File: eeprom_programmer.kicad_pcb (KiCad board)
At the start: 2 copper layers, 80 x 80 mm, 23 parts, among them J1 AVR ISP, J2 USB_B, SW1 Reset, U1 ATmega8-16PU, U2 MCP2221AxP, U3 74HC595, U4 74HC595, U5 28C256, Y1 7,3728MHz

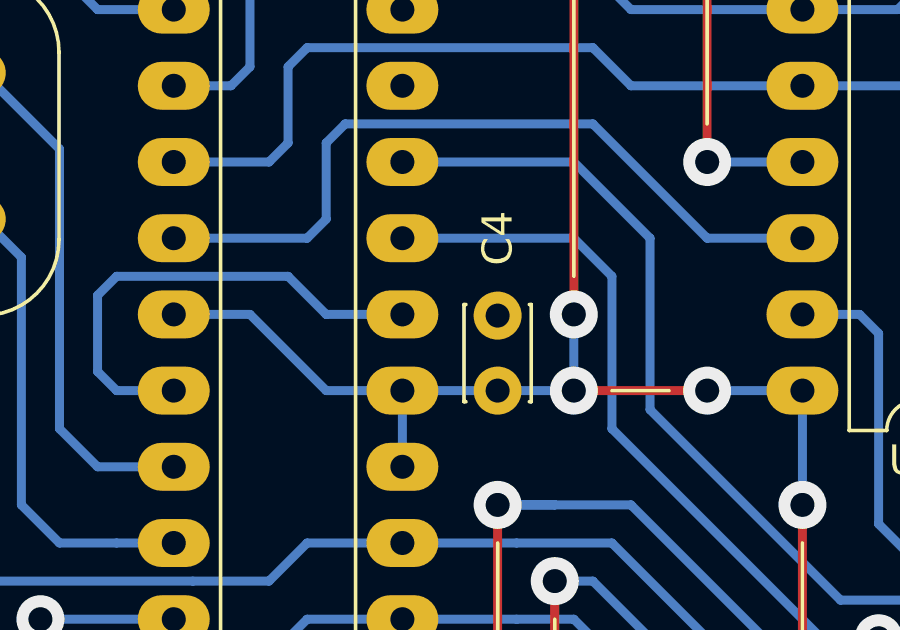
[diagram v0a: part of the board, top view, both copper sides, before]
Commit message: eeprom.py serial flush fix
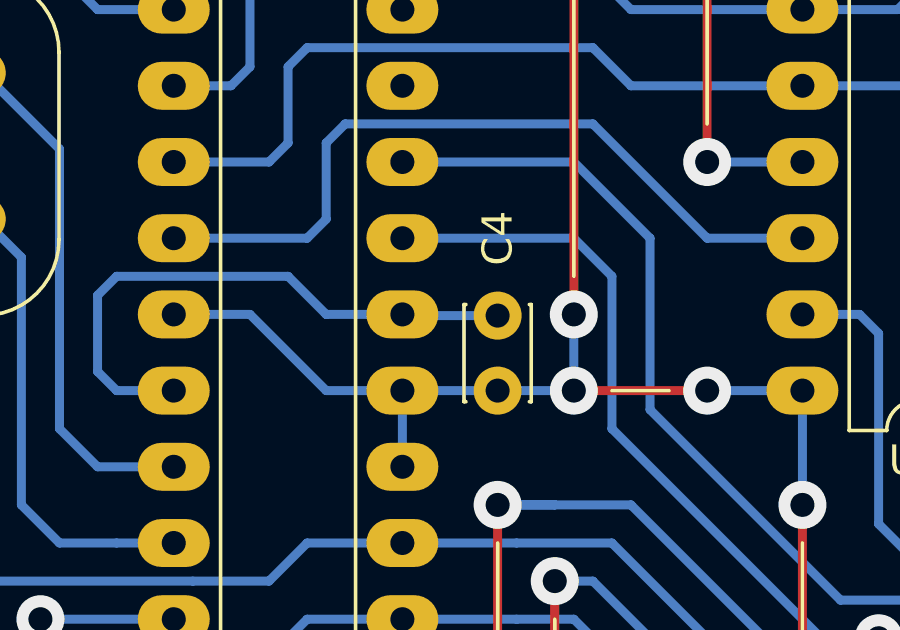
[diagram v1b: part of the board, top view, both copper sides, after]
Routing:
- net GND: track 167.2 -> 170.4 mm
